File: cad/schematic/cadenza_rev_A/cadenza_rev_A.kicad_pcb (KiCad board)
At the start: 2 copper layers, 80 x 50 mm, 33 parts, among them J2 USB_C_Receptacle, J3 Conn_01x02, Q1 BC547, U1 TLC5916, U10 HDSP-A151, U11 TLC5916, U12 HDSP-A151, U13 STM32F105RCTx, U14 INA193, U15 TLC5916, U2 HDSP-A151, U3 TLC5916, U4 HDSP-A151, U5 TLC5916, U6 HDSP-A151, U7 TLC5916, U8 HDSP-A151, U9 TLC5916

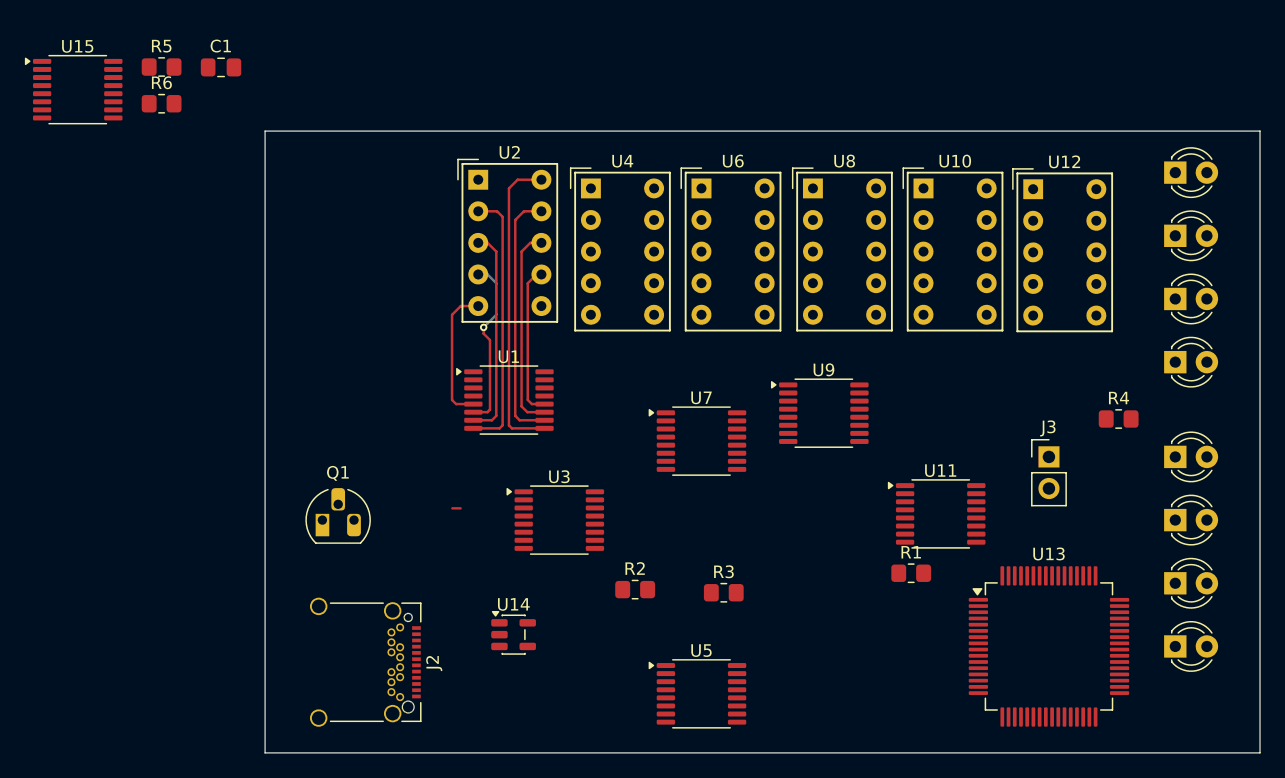
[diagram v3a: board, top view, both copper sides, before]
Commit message: upgraded to kicad 10
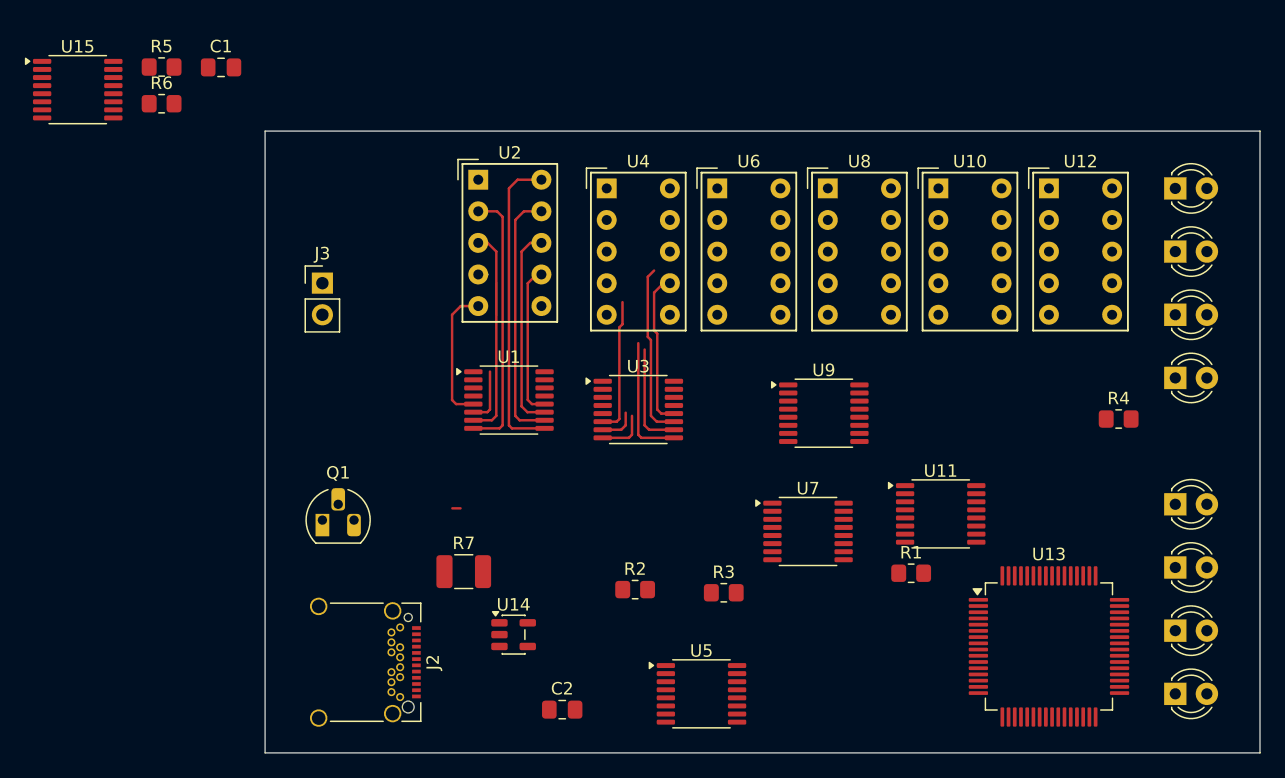
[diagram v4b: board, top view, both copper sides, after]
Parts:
- added C2: 100nF, Capacitor_SMD:C_0805_2012Metric_Pad1.18x1.45mm_HandSolder, F.Cu at (73.9, 96.5)
- added R7: 0.01, Resistor_SMD:R_1210_3225Metric_Pad1.30x2.65mm_HandSolder, F.Cu at (66.0, 85.4)
- moved J3 60.1 mm to (54.6, 62.2)
- moved U7 11.2 mm to (93.7, 82.2)
- moved U3 10.9 mm to (80.0, 72.4)
- moved D5 3.81 mm to (123.2, 80.0)
- moved D6 3.81 mm to (123.2, 85.1)
- moved D7 3.81 mm to (123.2, 90.2)
- moved D8 3.81 mm to (123.2, 95.2)
- moved U12 1.27 mm to (113.0, 54.6)
- moved D1 1.27 mm to (123.2, 54.6)
- moved D2 1.27 mm to (123.2, 59.7)
- moved D3 1.27 mm to (123.2, 64.8)
- moved D4 1.27 mm to (123.2, 69.8)
- moved U4 1.27 mm to (77.5, 54.6)
- moved U6 1.27 mm to (86.4, 54.6)
- moved U10 1.20 mm to (104.1, 54.6)
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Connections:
- C1 pad 1: unconnected-(C1-Pad1) -> +3.3V
- D1 pad 1: unconnected-(D1-K-Pad1) -> Net-(D1-K)
- D2 pad 1: unconnected-(D2-K-Pad1) -> Net-(D2-K)
- D3 pad 1: unconnected-(D3-K-Pad1) -> Net-(D3-K)
- D4 pad 1: unconnected-(D4-K-Pad1) -> Net-(D4-K)
- D5 pad 1: unconnected-(D5-K-Pad1) -> Net-(D5-K)
- D6 pad 1: unconnected-(D6-K-Pad1) -> Net-(D6-K)
- D7 pad 1: unconnected-(D7-K-Pad1) -> Net-(D7-K)
- D8 pad 1: unconnected-(D8-K-Pad1) -> Net-(D8-K)
- J2 pad A4: +5V -> Net-(U14-+)
- J2 pad A9: +5V -> Net-(U14-+)
- J2 pad B4: +5V -> Net-(U14-+)
- J2 pad B9: +5V -> Net-(U14-+)
- R5 pad 1: unconnected-(R5-Pad1) -> Net-(U13-BOOT0)
- R5 pad 2: unconnected-(R5-Pad2) -> GND
- U13 pad 60: unconnected-(U13-BOOT0-Pad60) -> Net-(U13-BOOT0)
- U13 pad 7: unconnected-(U13-NRST-Pad7) -> +3.3V
- U14 pad 2: unconnected-(U14-GND-Pad2) -> GND
- U14 pad 3: unconnected-(U14-+-Pad3) -> Net-(U14-+)
- U14 pad 4: unconnected-(U14---Pad4) -> +5V
- U14 pad 5: unconnected-(U14-V+-Pad5) -> +3.3V
- U15 pad 10: unconnected-(U15-~{OUT5}-Pad10) -> Net-(D6-K)
- U15 pad 11: unconnected-(U15-~{OUT6}-Pad11) -> Net-(D7-K)
- U15 pad 12: unconnected-(U15-~{OUT7}-Pad12) -> Net-(D8-K)
- U15 pad 5: unconnected-(U15-~{OUT0}-Pad5) -> Net-(D1-K)
- U15 pad 6: unconnected-(U15-~{OUT1}-Pad6) -> Net-(D2-K)
- U15 pad 7: unconnected-(U15-~{OUT2}-Pad7) -> Net-(D3-K)
- U15 pad 8: unconnected-(U15-~{OUT3}-Pad8) -> Net-(D4-K)
- U15 pad 9: unconnected-(U15-~{OUT4}-Pad9) -> Net-(D5-K)
- U3 pad 12: unconnected-(U3-~{OUT7}-Pad12) -> Net-(U3-~{OUT7})
- U4 pad 7: unconnected-(U4-DP-Pad7) -> Net-(U3-~{OUT7})
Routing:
- net unconnected-(U3-~{OUT6}-Pad11): track 0.00 -> 14.0 mm
- net Net-(U3-~{OUT7}): track 0.00 -> 12.6 mm
- net unconnected-(U3-~{OUT1}-Pad6): track 0.00 -> 10.9 mm
- net unconnected-(U3-~{OUT4}-Pad9): track 0.00 -> 10.3 mm
- net unconnected-(U3-~{OUT5}-Pad10): track 0.00 -> 8.60 mm
- net Net-(U1-~{OUT1}): track 14.0 -> 7.77 mm, vias 1 -> 0
- net unconnected-(U3-~{OUT3}-Pad8): track 0.00 -> 3.98 mm
- net unconnected-(U3-~{OUT2}-Pad7): track 0.00 -> 3.01 mm
